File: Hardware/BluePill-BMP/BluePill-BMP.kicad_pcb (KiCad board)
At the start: 2 copper layers, 70 x 60 mm, 23 parts, among them J1 Conn_01x07, J2 Conn_01x05, J3 Conn_01x11, J4 GDB_COMM, J5 VCC, J6 GND, J7 JTAG, J8 LogicAna, U1 FT232RL_Breakout, U2 STM32F103 BluePill

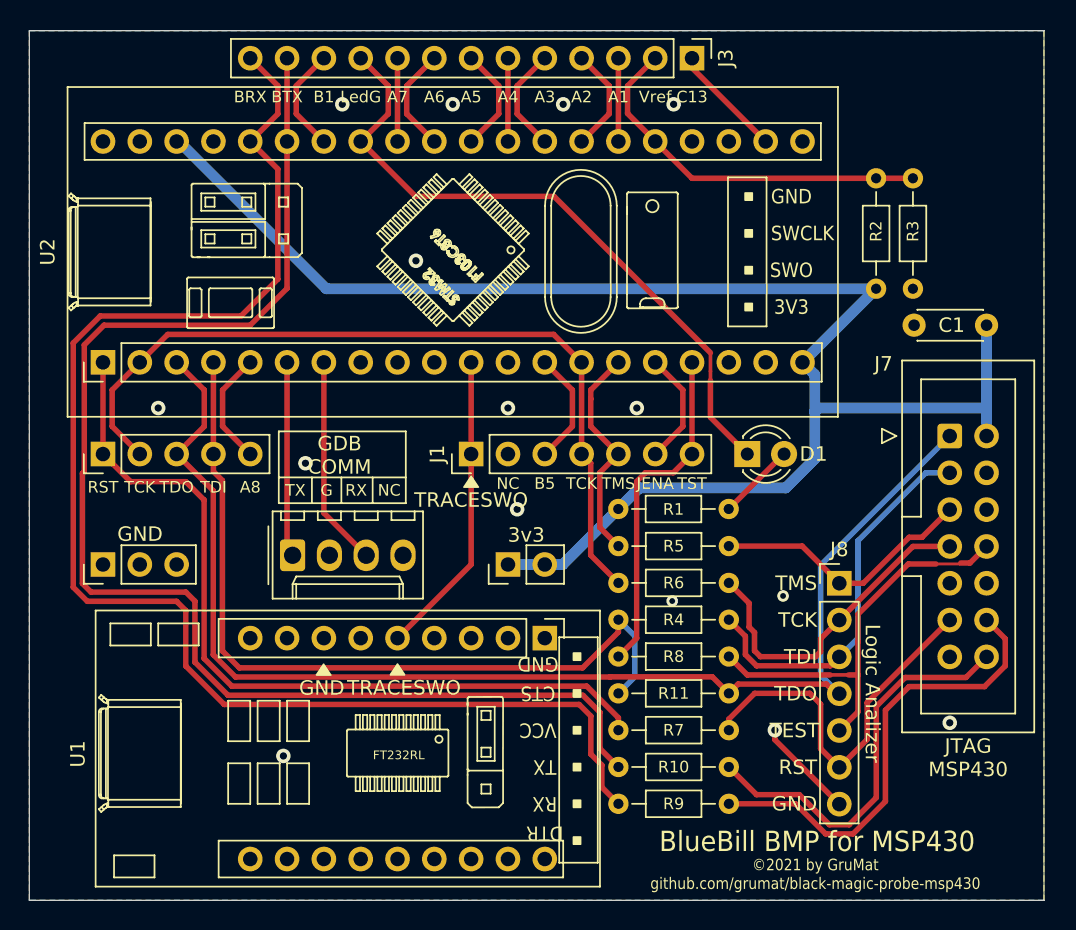
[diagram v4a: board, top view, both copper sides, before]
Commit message: BluePill Hardware: Swapped TIM4 Ch1 and Ch2 (reversed input and output) ass Ch2 input produces less delay, besides, simultaneous DMA access to the SPI2 is also possible.
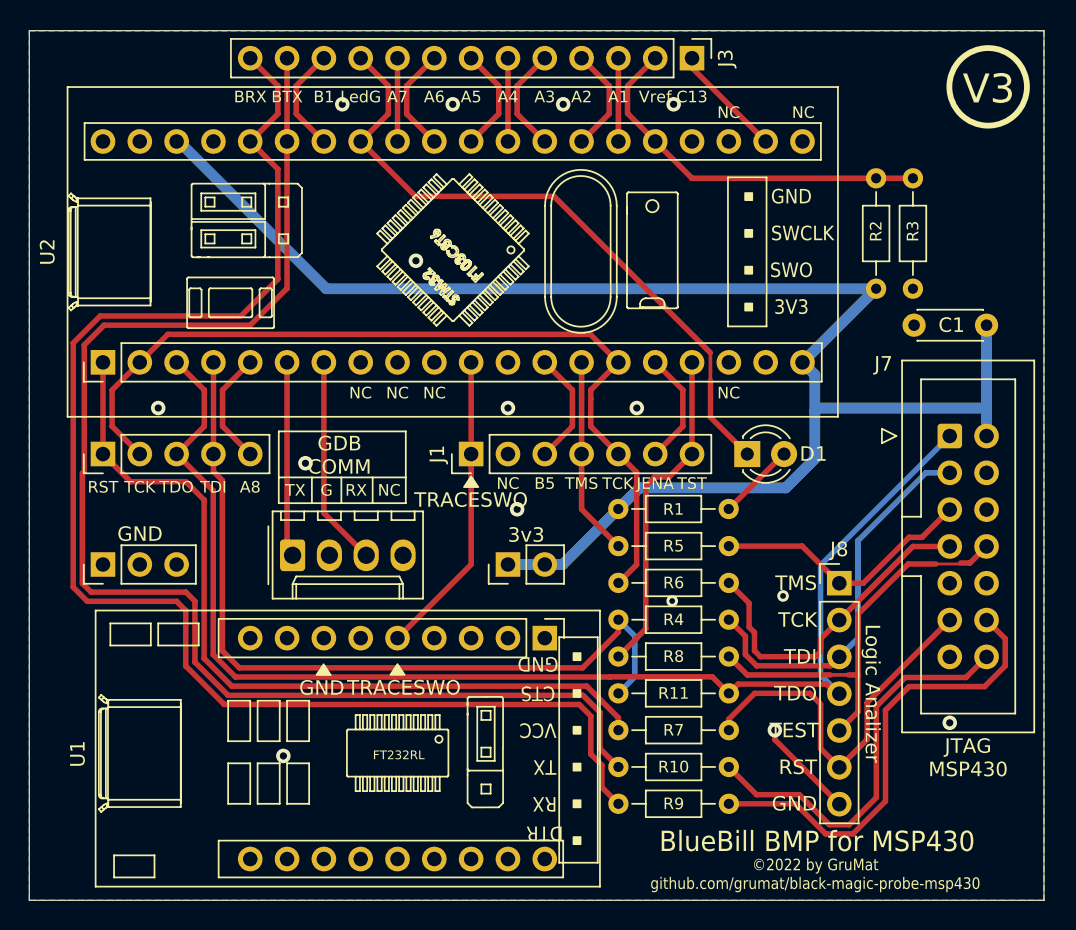
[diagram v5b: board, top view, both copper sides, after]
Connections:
- J1 pad 4: /BTCK -> /BTMS
- J1 pad 5: /BTMS -> /BTCK
- U2 pad 14: /BTCK -> /BTMS
- U2 pad 15: /BTMS -> /BTCK
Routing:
- net /BTCK: track 56.3 -> 60.4 mm
- net /BTMS: track 15.3 -> 13.7 mm
- net /BTEST: track 23.5 -> 23.0 mm
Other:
- board text added: "V3"
- board text added: "©2022 by GruMat github.com/grumat/black-magic-probe-msp430"
- board text removed: "©2021 by GruMat github.com/grumat/black-magic-probe-msp430"
